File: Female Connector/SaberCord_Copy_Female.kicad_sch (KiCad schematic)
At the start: 2 parts, among them J1 Conn_02x07_Row_Letter_Last, J2 Conn_02x12_Row_Letter_Last

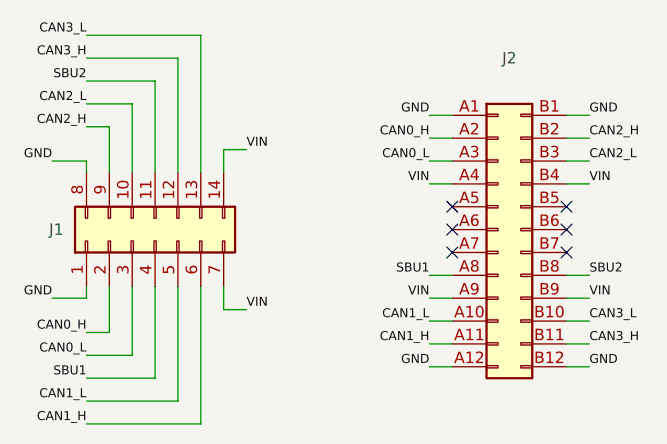
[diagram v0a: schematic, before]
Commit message: fusion360 possible, additional files added
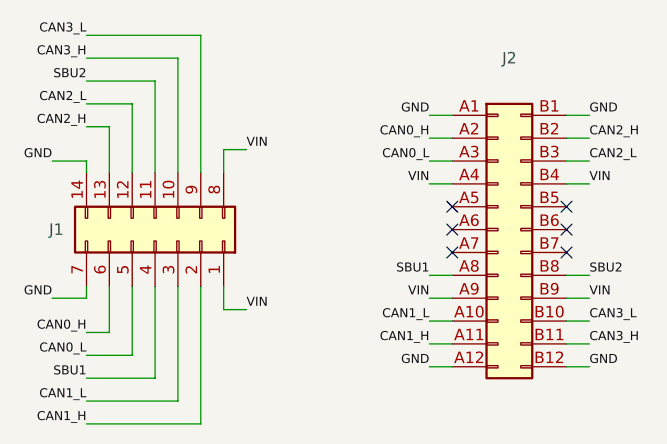
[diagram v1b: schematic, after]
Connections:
- net CAN0_H: now also J1.6 (Pin_6a); no longer J1.2 (Pin_2a)
- net CAN0_L: now also J1.5 (Pin_5a); no longer J1.3 (Pin_3a)
- net CAN1_H: now also J1.2 (Pin_2a); no longer J1.6 (Pin_6a)
- net CAN1_L: now also J1.3 (Pin_3a); no longer J1.5 (Pin_5a)
- net CAN2_H: now also J1.13 (Pin_6b); no longer J1.9 (Pin_2b)
- net CAN2_L: now also J1.12 (Pin_5b); no longer J1.10 (Pin_3b)
- net CAN3_H: now also J1.10 (Pin_3b); no longer J1.12 (Pin_5b)
- net CAN3_L: now also J1.9 (Pin_2b); no longer J1.13 (Pin_6b)
- net GND: now also J1.14 (Pin_7b), J1.7 (Pin_7a); no longer J1.1 (Pin_1a), J1.8 (Pin_1b)
- net VIN: now also J1.1 (Pin_1a), J1.8 (Pin_1b); no longer J1.14 (Pin_7b), J1.7 (Pin_7a)
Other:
- moved on the sheet: J1
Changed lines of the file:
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@@
     (stroke (width 0) (type default))
   )
-  (wire (pts (xy 146.05 62.23) (xy 146.05 57.15))
+  (wire (pts (xy 146.05 57.15) (xy 146.05 62.23))
     (stroke (width 0) (type default))
   )
   (wire (pts (xy 146.05 74.93) (xy 146.05 80.01))
-    (stroke (width 0) (type default))
-  )
-  (wire (pts (xy 151.13 62.23) (xy 151.13 52.07))
     (stroke (width 0) (type default))
   )
@@
   )
   (wire (pts (xy 181.61 81.28) (xy 184.15 81.28))
+    (stroke (width 0) (type default))
+  )
+  (wire (pts (xy 156.21 46.99) (xy 156.21 62.23))
     (stroke (width 0) (type default))
   )
@@
     (stroke (width 0) (type default))
   )
+  (wire (pts (xy 151.13 52.07) (xy 151.13 62.23))
+    (stroke (width 0) (type default))
+  )
   (wire (pts (xy 139.7 76.2) (xy 143.51 76.2))
     (stroke (width 0) (type default))
   )
-  (wire (pts (xy 148.59 62.23) (xy 148.59 54.61))
+  (wire (pts (xy 148.59 54.61) (xy 148.59 62.23))
     (stroke (width 0) (type default))
   )
@@
     (stroke (width 0) (type default))
   )
-  (wire (pts (xy 156.21 62.23) (xy 156.21 46.99))
-    (stroke (width 0) (type default))
-  )
   (wire (pts (xy 196.85 81.28) (xy 199.39 81.28))
     (stroke (width 0) (type default))
@@
     (stroke (width 0) (type default))
   )
-  (wire (pts (xy 153.67 62.23) (xy 153.67 49.53))
+  (wire (pts (xy 153.67 49.53) (xy 153.67 62.23))
     (stroke (width 0) (type default))
   )
@@
     (effects (font (size 1 1)) (justify left bottom))
   )
-  (symbol (lib_id "Connector_Generic:Conn_02x07_Row_Letter_Last") (at 151.13 69.85 90) (unit 1)
-    (in_bom yes) (on_board yes) (dnp no) (fields_autoplaced)
+  (symbol (lib_id "Connector_Generic:Conn_02x07_Row_Letter_Last") (at 151.13 69.85 270) (mirror x) (unit 1)
+    (in_bom yes) (on_board yes) (dnp no)
     (property "Reference" "J1" (at 140.97 68.58 90)
-      (effects (font (size 1.27 1.27)) (justify left))
+      (effects (font (size 1.27 1.27)) (justify right))
     )
-    (property "Value" "Conn_02x07_Row_Letter_Last" (at 139.7 68.58 0)
+    (property "Value" "Conn_02x07_Row_Letter_Last" (at 162.56 68.58 0)
       (effects (font (size 1.27 1.27)) hide)
     )

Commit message: fixed female connector mirror
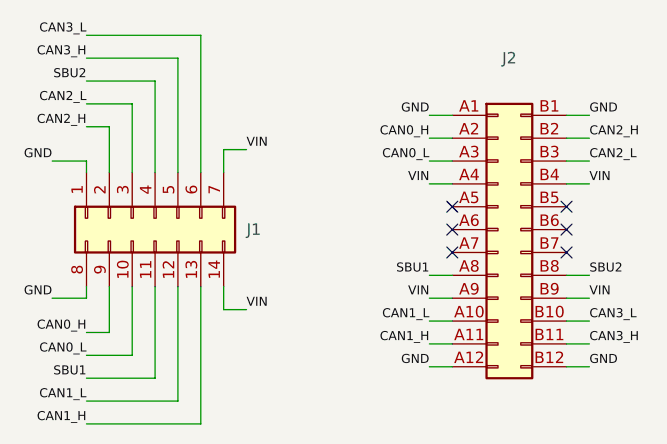
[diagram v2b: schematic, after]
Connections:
- net CAN0_H: now also J1.9 (Pin_2b); no longer J1.6 (Pin_6a)
- net CAN0_L: now also J1.10 (Pin_3b); no longer J1.5 (Pin_5a)
- net CAN1_H: now also J1.13 (Pin_6b); no longer J1.2 (Pin_2a)
- net CAN1_L: now also J1.12 (Pin_5b); no longer J1.3 (Pin_3a)
- net CAN2_H: now also J1.2 (Pin_2a); no longer J1.13 (Pin_6b)
- net CAN2_L: now also J1.3 (Pin_3a); no longer J1.12 (Pin_5b)
- net CAN3_H: now also J1.5 (Pin_5a); no longer J1.10 (Pin_3b)
- net CAN3_L: now also J1.6 (Pin_6a); no longer J1.9 (Pin_2b)
- net GND: now also J1.1 (Pin_1a), J1.8 (Pin_1b); no longer J1.14 (Pin_7b), J1.7 (Pin_7a)
- net SBU1: now also J1.11 (Pin_4b); no longer J1.4 (Pin_4a)
- net SBU2: now also J1.4 (Pin_4a); no longer J1.11 (Pin_4b)
- net VIN: now also J1.14 (Pin_7b), J1.7 (Pin_7a); no longer J1.1 (Pin_1a), J1.8 (Pin_1b)
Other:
- moved on the sheet: J1
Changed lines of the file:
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@@
   (no_connect (at 184.15 66.04))
   (no_connect (at 184.15 68.58))
+  (wire (pts (xy 146.05 74.93) (xy 146.05 80.01))
+    (stroke (width 0) (type default))
+  )
   (wire (pts (xy 181.61 60.96) (xy 184.15 60.96))
     (stroke (width 0) (type default))
@@
     (stroke (width 0) (type default))
   )
+  (wire (pts (xy 153.67 74.93) (xy 153.67 87.63))
+    (stroke (width 0) (type default))
+  )
   (wire (pts (xy 151.13 52.07) (xy 143.51 52.07))
     (stroke (width 0) (type default))
@@
     (stroke (width 0) (type default))
   )
-  (wire (pts (xy 146.05 74.93) (xy 146.05 80.01))
+  (wire (pts (xy 181.61 78.74) (xy 184.15 78.74))
+    (stroke (width 0) (type default))
+  )
+  (wire (pts (xy 181.61 81.28) (xy 184.15 81.28))
+    (stroke (width 0) (type default))
+  )
+  (wire (pts (xy 156.21 46.99) (xy 156.21 62.23))
+    (stroke (width 0) (type default))
+  )
+  (wire (pts (xy 158.75 59.69) (xy 161.29 59.69))
+    (stroke (width 0) (type default))
+  )
+  (wire (pts (xy 181.61 83.82) (xy 184.15 83.82))
+    (stroke (width 0) (type default))
+  )
+  (wire (pts (xy 143.51 57.15) (xy 146.05 57.15))
+    (stroke (width 0) (type default))
+  )
+  (wire (pts (xy 158.75 77.47) (xy 161.29 77.47))
+    (stroke (width 0) (type default))
+  )
+  (wire (pts (xy 151.13 52.07) (xy 151.13 62.23))
+    (stroke (width 0) (type default))
+  )
+  (wire (pts (xy 139.7 76.2) (xy 143.51 76.2))
+    (stroke (width 0) (type default))
+  )
+  (wire (pts (xy 148.59 54.61) (xy 148.59 62.23))
+    (stroke (width 0) (type default))
+  )
+  (wire (pts (xy 156.21 46.99) (xy 143.51 46.99))
+    (stroke (width 0) (type default))
+  )
+  (wire (pts (xy 151.13 74.93) (xy 151.13 85.09))
+    (stroke (width 0) (type default))
+  )
+  (wire (pts (xy 181.61 63.5) (xy 184.15 63.5))
+    (stroke (width 0) (type default))
+  )
+  (wire (pts (xy 196.85 81.28) (xy 199.39 81.28))
+    (stroke (width 0) (type default))
+  )
+  (wire (pts (xy 153.67 49.53) (xy 153.67 62.23))
+    (stroke (width 0) (type default))
+  )
+  (wire (pts (xy 156.21 90.17) (xy 143.51 90.17))
+    (stroke (width 0) (type default))
+  )
+  (wire (pts (xy 196.85 55.88) (xy 199.39 55.88))
     (stroke (width 0) (type default))
   )
@@
     (stroke (width 0) (type default))
   )
-  (wire (pts (xy 181.61 78.74) (xy 184.15 78.74))
-    (stroke (width 0) (type default))
-  )
-  (wire (pts (xy 181.61 81.28) (xy 184.15 81.28))
-    (stroke (width 0) (type default))
-  )
-  (wire (pts (xy 156.21 46.99) (xy 156.21 62.23))
-    (stroke (width 0) (type default))
-  )
-  (wire (pts (xy 158.75 59.69) (xy 161.29 59.69))
-    (stroke (width 0) (type default))
-  )
-  (wire (pts (xy 181.61 83.82) (xy 184.15 83.82))
-    (stroke (width 0) (type default))
-  )
-  (wire (pts (xy 143.51 57.15) (xy 146.05 57.15))
-    (stroke (width 0) (type default))
-  )
-  (wire (pts (xy 158.75 77.47) (xy 161.29 77.47))
-    (stroke (width 0) (type default))
-  )
-  (wire (pts (xy 153.67 74.93) (xy 153.67 87.63))
-    (stroke (width 0) (type default))
-  )
-  (wire (pts (xy 151.13 52.07) (xy 151.13 62.23))
-    (stroke (width 0) (type default))
-  )
-  (wire (pts (xy 139.7 76.2) (xy 143.51 76.2))
-    (stroke (width 0) (type default))
-  )
-  (wire (pts (xy 148.59 54.61) (xy 148.59 62.23))
-    (stroke (width 0) (type default))
-  )
-  (wire (pts (xy 156.21 46.99) (xy 143.51 46.99))
-    (stroke (width 0) (type default))
-  )
-  (wire (pts (xy 181.61 63.5) (xy 184.15 63.5))
-    (stroke (width 0) (type default))
-  )
-  (wire (pts (xy 196.85 81.28) (xy 199.39 81.28))
+  (wire (pts (xy 181.61 73.66) (xy 184.15 73.66))
+    (stroke (width 0) (type default))
+  )
+  (wire (pts (xy 196.85 60.96) (xy 199.39 60.96))
+    (stroke (width 0) (type default))
+  )
+  (wire (pts (xy 196.85 78.74) (xy 199.39 78.74))
+    (stroke (width 0) (type default))
+  )
+  (wire (pts (xy 139.7 60.96) (xy 143.51 60.96))
     (stroke (width 0) (type default))
   )
@@
     (stroke (width 0) (type default))
   )
-  (wire (pts (xy 153.67 49.53) (xy 153.67 62.23))
-    (stroke (width 0) (type default))
-  )
-  (wire (pts (xy 156.21 90.17) (xy 143.51 90.17))
-    (stroke (width 0) (type default))
-  )
-  (wire (pts (xy 196.85 55.88) (xy 199.39 55.88))
-    (stroke (width 0) (type default))
-  )
-  (wire (pts (xy 181.61 73.66) (xy 184.15 73.66))
-    (stroke (width 0) (type default))
-  )
-  (wire (pts (xy 196.85 60.96) (xy 199.39 60.96))
-    (stroke (width 0) (type default))
-  )
-  (wire (pts (xy 151.13 74.93) (xy 151.13 85.09))
-    (stroke (width 0) (type default))
-  )
-  (wire (pts (xy 196.85 78.74) (xy 199.39 78.74))
-    (stroke (width 0) (type default))
-  )
-  (wire (pts (xy 139.7 60.96) (xy 143.51 60.96))
-    (stroke (width 0) (type default))
-  )
   (wire (pts (xy 196.85 76.2) (xy 199.39 76.2))
     (stroke (width 0) (type default))
@@
     (effects (font (size 1 1)) (justify left bottom))
   )
-  (symbol (lib_id "Connector_Generic:Conn_02x07_Row_Letter_Last") (at 151.13 69.85 270) (mirror x) (unit 1)
+  (symbol (lib_id "Connector_Generic:Conn_02x07_Row_Letter_Last") (at 151.13 67.31 90) (mirror x) (unit 1)
     (in_bom yes) (on_board yes) (dnp no)
-    (property "Reference" "J1" (at 140.97 68.58 90)
+    (property "Reference" "J1" (at 161.29 68.58 90)
       (effects (font (size 1.27 1.27)) (justify right))
     )
-    (property "Value" "Conn_02x07_Row_Letter_Last" (at 162.56 68.58 0)
+    (property "Value" "Conn_02x07_Row_Letter_Last" (at 139.7 68.58 0)
       (effects (font (size 1.27 1.27)) hide)
     )
-    (property "Footprint" "CommaPogo_Library:2x7_Pogo_Female" (at 151.13 69.85 0)
+    (property "Footprint" "CommaPogo_Library:2x7_Pogo_Female" (at 151.13 67.31 0)
       (effects (font (size 1.27 1.27)) hide)
     )
-    (property "Datasheet" "~" (at 151.13 69.85 0)
+    (property "Datasheet" "~" (at 151.13 67.31 0)
       (effects (font (size 1.27 1.27)) hide)
     )
